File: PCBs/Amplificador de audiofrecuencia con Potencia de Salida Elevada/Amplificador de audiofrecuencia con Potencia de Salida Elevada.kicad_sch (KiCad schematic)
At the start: 29 parts, among them Q1 2N331, Q2 2N331, Q3 2N331, Q4 2N331

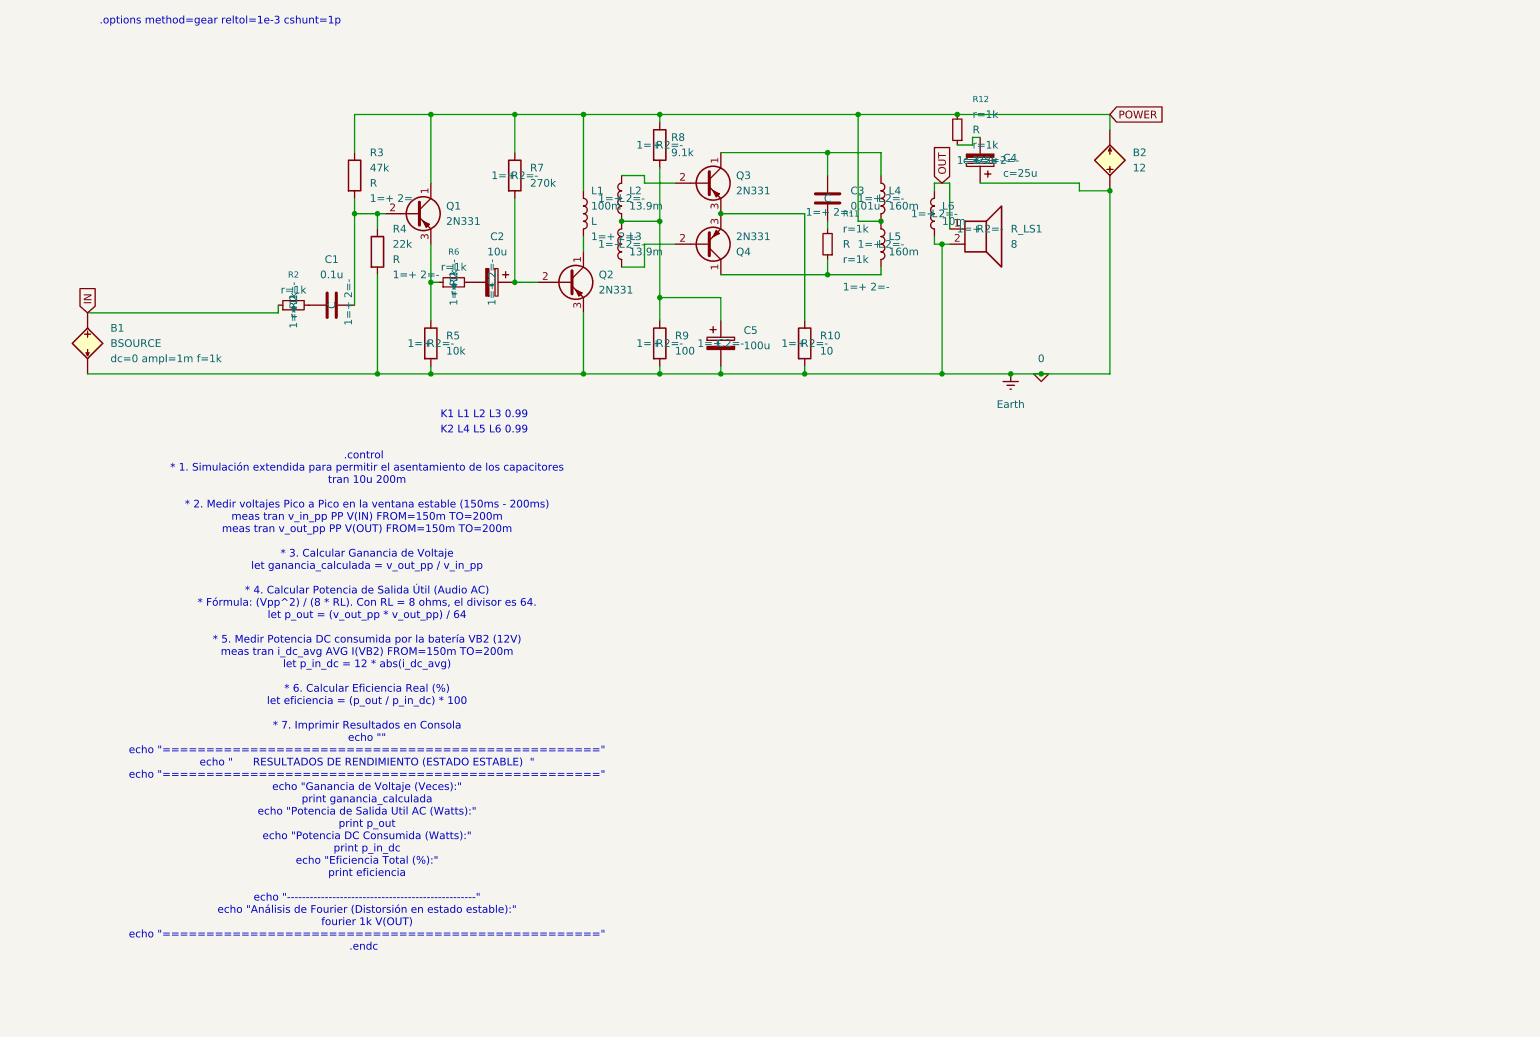
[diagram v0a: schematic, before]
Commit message: Se creó una nueva version del Amplificador simple, siendo seleccionado como amplificador final, se creó el circuito del detector sin embargo no fue testeado por la dificultad de crear una simulación para un detector AM
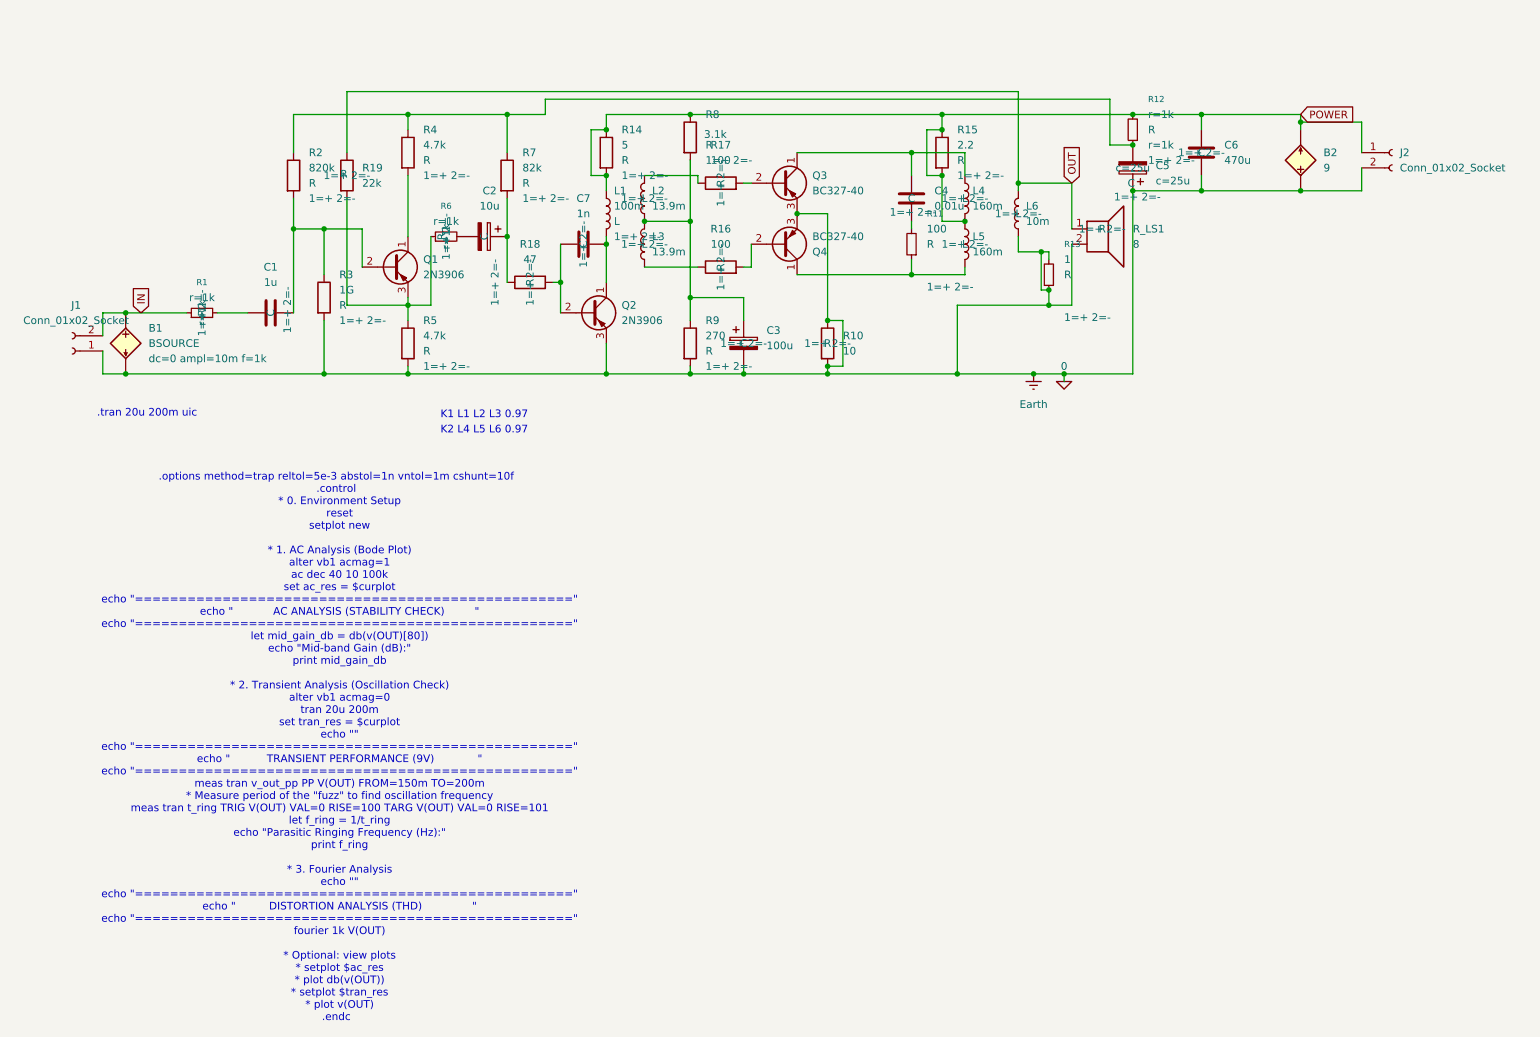
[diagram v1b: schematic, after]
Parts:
- added C6: 470u, Capacitor_THT:C_Radial_D5.0mm_H11.0mm_P2.00mm, symbol Device:C
- added C7: 1n, Capacitor_THT:C_Radial_D5.0mm_H11.0mm_P2.00mm, symbol Device:C
- added J1, J2: Conn_01x02_Socket, Connector_TE-Connectivity:TE_826576-2_1x02_P3.96mm_Vertical, symbol Connector:Conn_01x02_Socket
- added R13: 1, symbol Device:R_Small
- added R14: 5, symbol Device:R
- added R15: 2.2, symbol Device:R
- added R16, R17: 100, Resistor_THT:R_Axial_DIN0207_L6.3mm_D2.5mm_P10.16mm_Horizontal, symbol Device:R
- added R18: 47, Resistor_THT:R_Axial_DIN0207_L6.3mm_D2.5mm_P10.16mm_Horizontal, symbol Device:R
- added R19: 22k, Resistor_THT:R_Axial_DIN0207_L6.3mm_D2.5mm_P10.16mm_Horizontal, symbol Device:R
- added R4: 4.7k, Resistor_THT:R_Axial_DIN0207_L6.3mm_D2.5mm_P10.16mm_Horizontal, symbol Device:R
- B2: value 12 -> 9
- C1: value 0.1u -> 1u; footprint (none) -> Capacitor_THT:C_Radial_D5.0mm_H11.0mm_P2.00mm
- C2: footprint (none) -> Capacitor_THT:C_Radial_D5.0mm_H11.0mm_P2.00mm
- C3: renamed from C5; footprint (none) -> Capacitor_THT:C_Radial_D5.0mm_H11.0mm_P2.00mm
- C4: renamed from C3; footprint (none) -> Capacitor_THT:C_Radial_D5.0mm_H11.0mm_P2.00mm
- C5: renamed from C4; footprint (none) -> Capacitor_THT:C_Radial_D5.0mm_H11.0mm_P2.00mm
- L1, L2, L3, L4, L5, L6: footprint (none) -> Inductor_THT:L_Axial_L7.0mm_D3.3mm_P10.16mm_Horizontal_Fastron_MICC
- Q1, Q2: value 2N331 -> 2N3906; footprint (none) -> Package_TO_SOT_THT:TO-92L_Inline
- Q3, Q4: value 2N331 -> BC327-40; footprint (none) -> Package_TO_SOT_THT:TO-92L_Inline
- R1: renamed from R2; footprint (none) -> Resistor_THT:R_Axial_DIN0207_L6.3mm_D2.5mm_P10.16mm_Horizontal
- R11: value ${SIM.PARAMS} -> 100; footprint (none) -> Resistor_THT:R_Axial_DIN0207_L6.3mm_D2.5mm_P10.16mm_Horizontal
- R12, R6: footprint (none) -> Resistor_THT:R_Axial_DIN0207_L6.3mm_D2.5mm_P10.16mm_Horizontal
- R2: renamed from R3; value 47k -> 820k; footprint (none) -> Resistor_THT:R_Axial_DIN0207_L6.3mm_D2.5mm_P10.16mm_Horizontal
- R3: renamed from R4; value 22k -> 1G; footprint (none) -> Resistor_THT:R_Axial_DIN0207_L6.3mm_D2.5mm_P10.16mm_Horizontal
- R5: value 10k -> 4.7k; footprint (none) -> Resistor_THT:R_Axial_DIN0207_L6.3mm_D2.5mm_P10.16mm_Horizontal
- R7: value 270k -> 82k; footprint (none) -> Resistor_THT:R_Axial_DIN0207_L6.3mm_D2.5mm_P10.16mm_Horizontal
- R8: value 9.1k -> 3.1k; footprint (none) -> Resistor_THT:R_Axial_DIN0207_L6.3mm_D2.5mm_P10.16mm_Horizontal
- R9: value 100 -> 270; footprint (none) -> Resistor_THT:R_Axial_DIN0207_L6.3mm_D2.5mm_P10.16mm_Horizontal
- R_LS1: footprint (none) -> Connector_TE-Connectivity:TE_826576-2_1x02_P3.96mm_Vertical
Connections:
- net 0: now also Q3.3 (E), Q4.3 (E), R10.1, C6.2, J1.1 (Pin_1), J2.2 (Pin_2), R13.1, R13.2
- net IN: now also J1.2 (Pin_2)
- net OUT: now also R19.1
- net POWER: now also C6.1, J2.1 (Pin_1), R14.1, R14.2, R15.1, R15.2; no longer Q1.1 (C), R2.1, R7.1
- net at Q1.3 (E), R5.1, R6.1: now also R19.2
- net at C5.2, R12.1: now also R2.1, R7.1, R4.1
- net at L3.1: now also R16.1; no longer Q4.2 (B)
- net at C2.1, R7.2: now also R18.1; no longer Q2.2 (B)
- net at L2.2: now also R17.1; no longer Q3.2 (B)
- net at L1.2, Q2.1 (C): now also C7.2
- new net: Q1.1 (C), R4.2
- new net: C7.1, Q2.2 (B), R18.2
- new net: Q4.2 (B), R16.2
- new net: Q3.2 (B), R17.2
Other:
- note added: ".options method=trap reltol=5e-3 abstol=1n vntol=1m cshunt=10f .control * 0. Environment Setup reset setplot new * 1. AC Analysis (Bode Plot) alter vb1 acmag=1 ac dec 40 10 100k set ac_res = $curplot echo "==================================================" echo " AC ANALYSIS (STABILITY CHECK) " echo "==================================================" let mid_gain_db = db(v(OUT)[80]) echo "Mid-b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"
- note added: ".tran 20u 200m uic"
- note added: "K1 L1 L2 L3 0.97"
- note added: "K2 L4 L5 L6 0.97"
- note removed: ".control * 1. Simulación extendida para permitir el asentamiento de los capacitores tran 10u 200m * 2. Medir voltajes Pico a Pico en la ventana estable (150ms - 200ms) meas tran v_in_pp PP V(IN) FROM=150m TO=200m meas tran v_out_pp PP V(OUT) FROM=150m TO=200m * 3. Calcular Ganancia de Voltaje let ganancia_calculada = v_out_pp / v_in_pp * 4. Calcular Potencia de Salida Útil (Audio AC) * Fórmula: (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"
- note removed: ".options method=gear reltol=1e-3 cshunt=1p"
- note removed: "K1 L1 L2 L3 0.99"
- note removed: "K2 L4 L5 L6 0.99"
- moved on the sheet: B1, B2, C1, C2, C3, C4, C5, L1, L2, L3, L4, L5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
